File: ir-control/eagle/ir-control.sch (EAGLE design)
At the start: 35 parts, among them J1 MICRO USB, J2 MICRO USB, J3 MICRO USB, J4 SJ1-3523NG, Q1 DTA114EET1G (2x10K), Q2 12Mhz, Q3 MMBT2222A, U1 NUF2042XV6T1G, U2 MCP1754ST-3302E/CB, U3 LPC11U35FHI33/501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

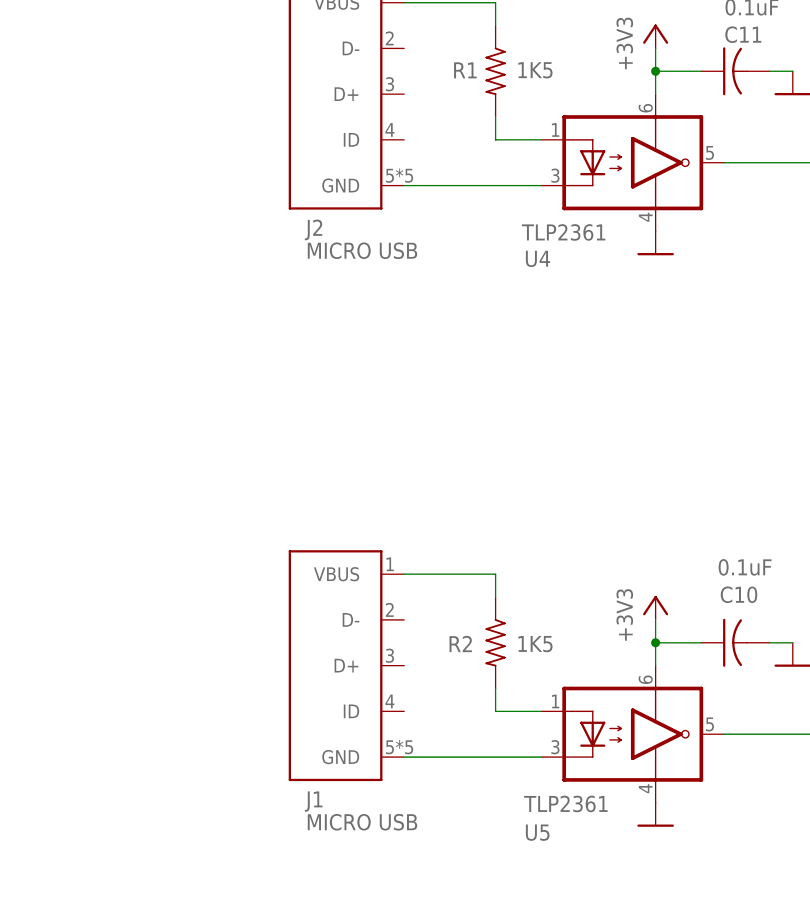
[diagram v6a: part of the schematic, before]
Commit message: Removed the shield connection of the sense connectors.
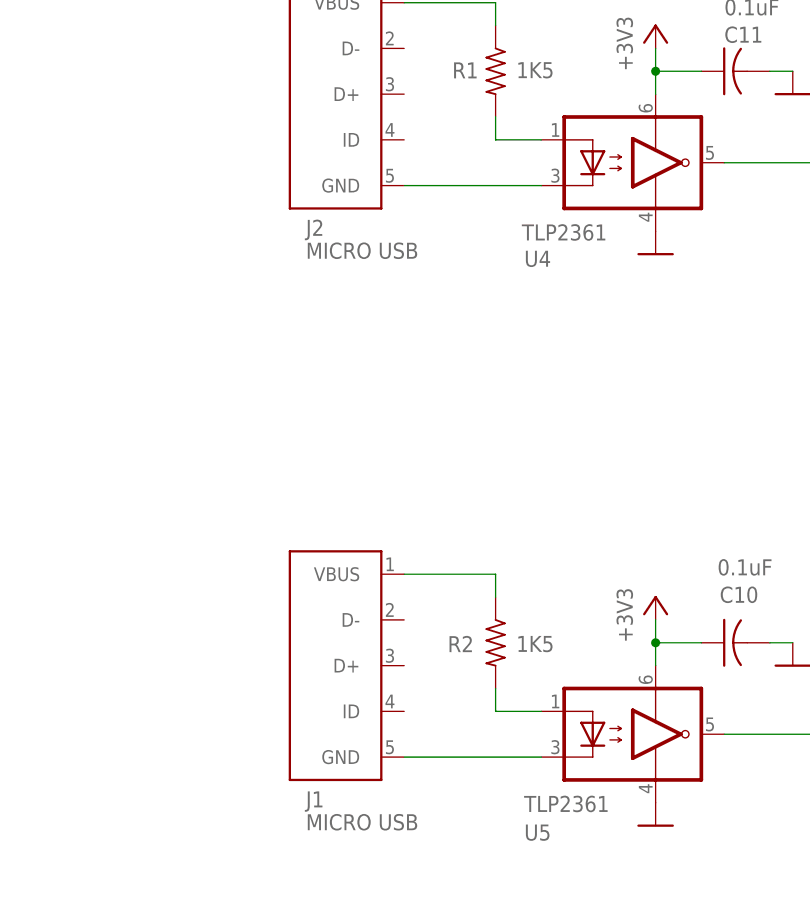
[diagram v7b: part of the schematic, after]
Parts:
- J1, J2: device ir-control:USB-CONN -> ir-control:USB-CONN-UNSHIELDED
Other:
- moved on the sheet: J1, J2
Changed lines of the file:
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@@
 <part name="C4" library="ir-control" deviceset="C" device="C0805K" value="10u"/>
 <part name="U2" library="ir-control" deviceset="LDO" device="" value="MCP1754ST-3302E/CB"/>
-<part name="J2" library="ir-control" deviceset="USB-CONN" device="" value="MICRO USB"/>
-<part name="J1" library="ir-control" deviceset="USB-CONN" device="" value="MICRO USB"/>
+<part name="J2" library="ir-control" deviceset="USB-CONN-UNSHIELDED" device="" value="MICRO USB"/>
+<part name="J1" library="ir-control" deviceset="USB-CONN-UNSHIELDED" device="" value="MICRO USB"/>
 <part name="R2" library="ir-control" deviceset="R" device="R0402" value="1K5"/>
 <part name="J4" library="ir-control" deviceset="JACK" device="X" value="SJ1-3523NG"/>

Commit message: Removed connection to av/tv shields.
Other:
- moved on the sheet: C1, C10, C11, C2, C3, C4, C5, C6, C7, C8, C9, D1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
